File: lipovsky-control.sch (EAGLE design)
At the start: 46 parts, among them J1 JUMPER-PAD, P1 M04-929P, P2 M04-929P, P3 M04-929P, P4 M04-929P, U1 ATTINYX4A8MU, U2 MIC2288YD5, U3 MIC2288YD5, U4 LTV-816S

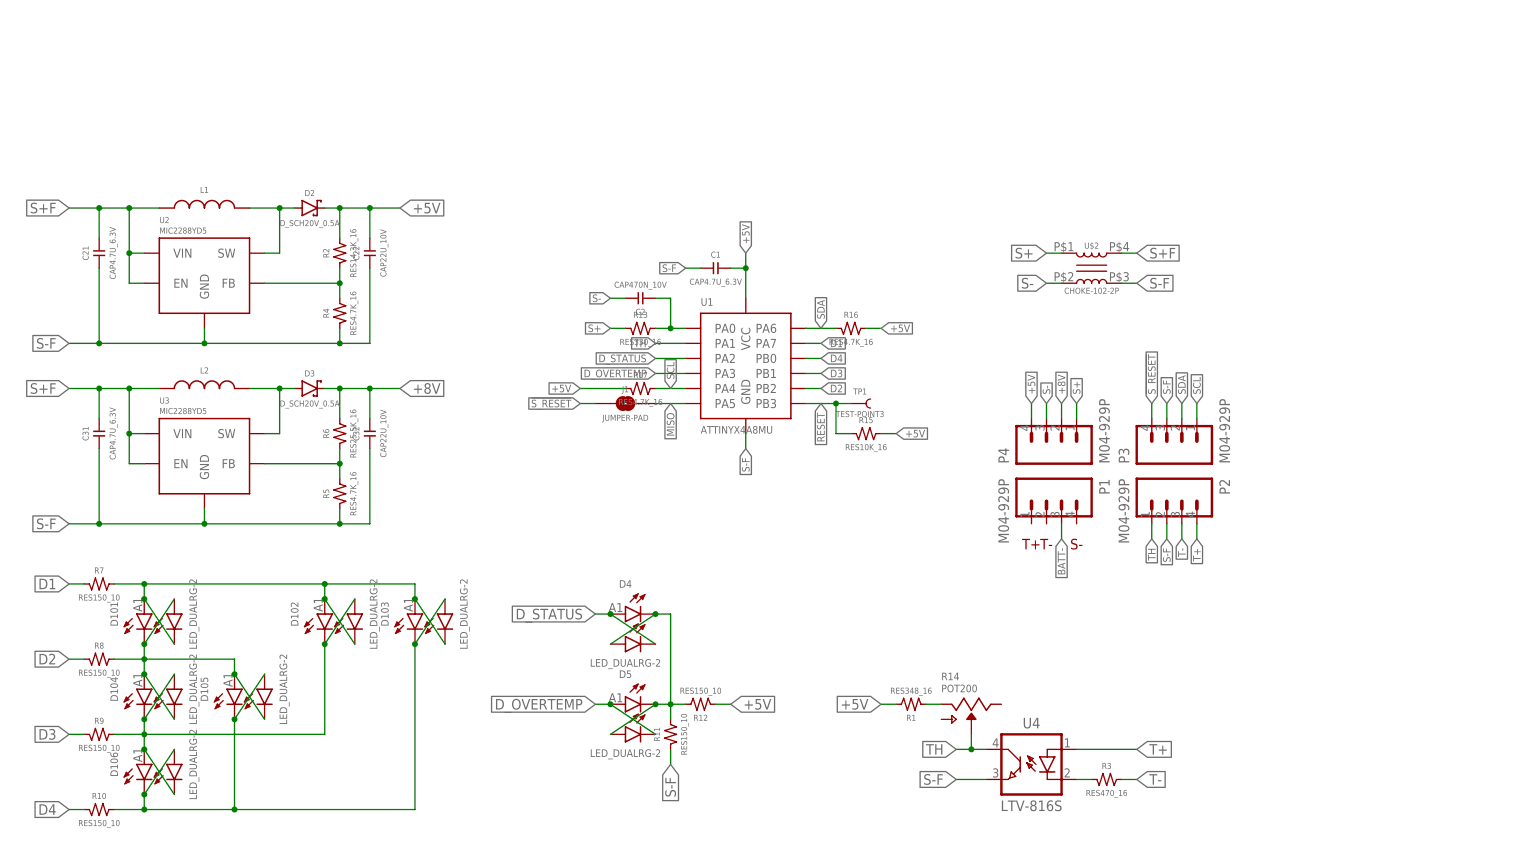
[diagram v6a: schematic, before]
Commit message: prog testpoints
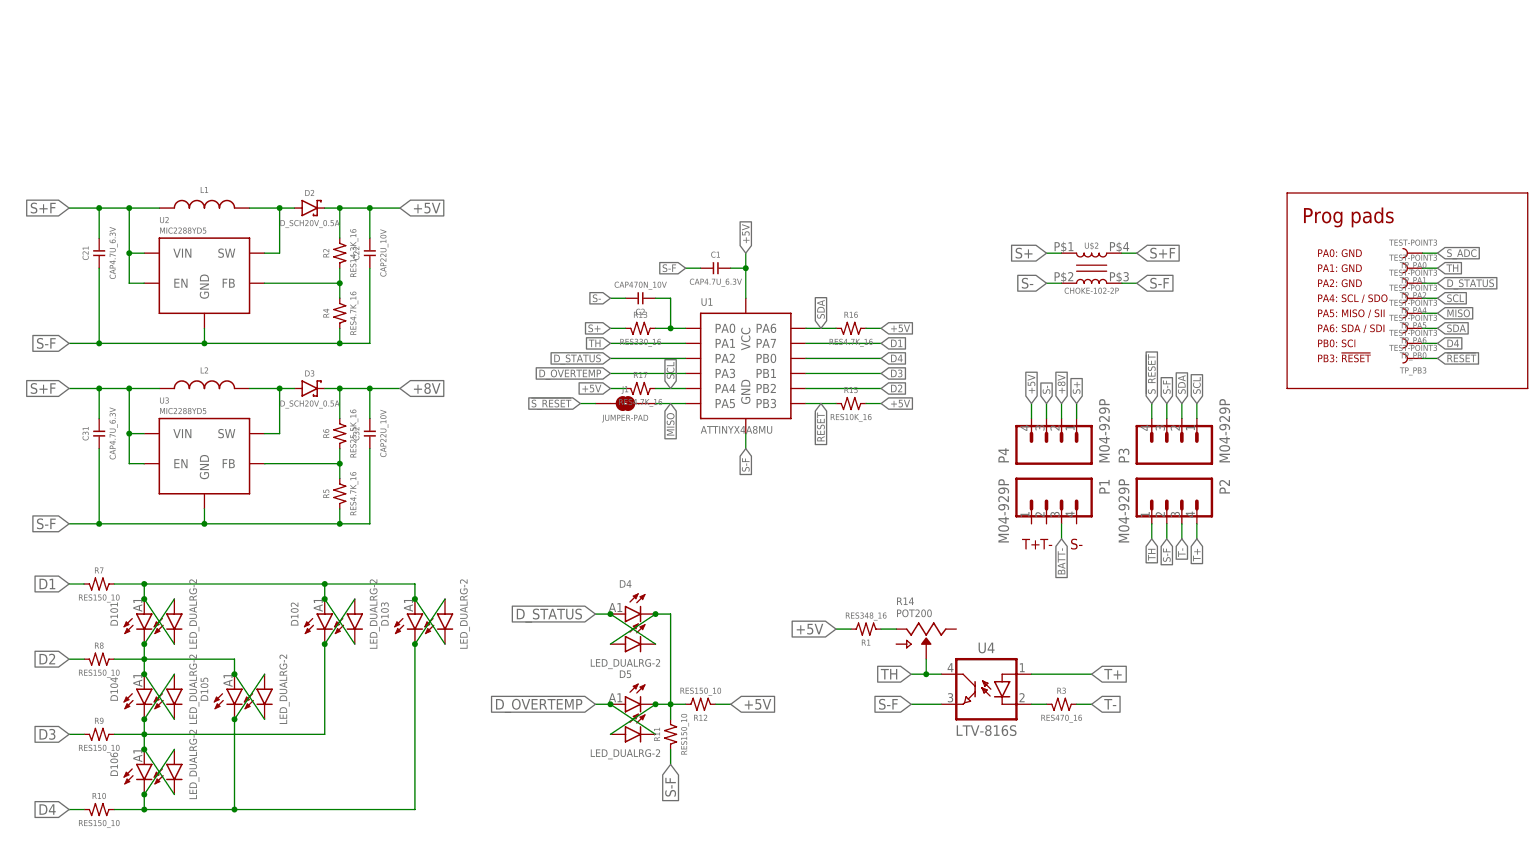
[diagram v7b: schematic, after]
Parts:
- removed TP1: TEST-POINT3, SparkFun-Passives:TEST-POINT3
- added TP_PA0, TP_PA1, TP_PA2, TP_PA4, TP_PA5, TP_PA6, TP_PB0, TP_PB3: TEST-POINT3, SparkFun-Passives:TEST-POINT3
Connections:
- net !RESET: now also TP_PB3.1; no longer TP1.1
- net D4: now also TP_PB0.1
- net D_STATUS: now also TP_PA2.1
- net MISO: now also TP_PA5.1
- net SCL: now also TP_PA4.1
- net SDA: now also TP_PA6.1
- net S_ADC: now also TP_PA0.1
- net TH: now also TP_PA1.1
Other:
- note added: "PA0: GND"
- note added: "PA1: GND"
- note added: "PA2: GND"
- note added: "PA4: SCL / SDO"
- note added: "PA5: MISO / SII"
- note added: "PA6: SDA / SDI"
- note added: "PB0: SCI"
- note added: "PB3: !RESET"
- note added: "Prog pads"
- moved on the sheet: R1, R14, R15, R3, U4

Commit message: ATtiny1616
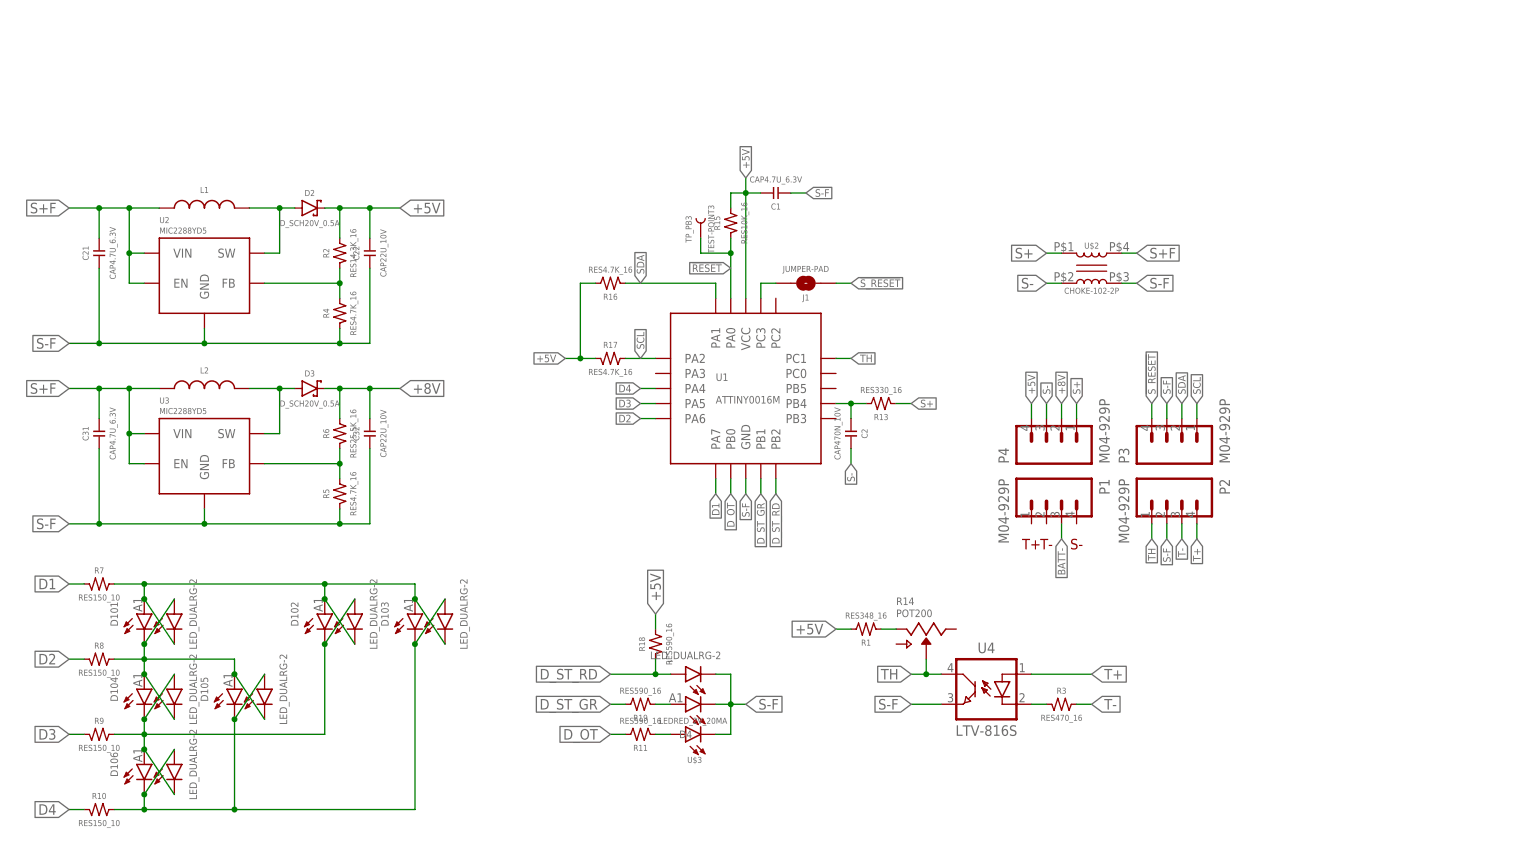
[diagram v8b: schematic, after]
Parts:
- removed D5: LED_DUALRG-2, dubec:LED_DUALRG-2
- removed R12: RES150_10, dubec:RES150_10
- removed TP_PA0, TP_PA1, TP_PA2, TP_PA4, TP_PA5, TP_PA6, TP_PB0: TEST-POINT3, SparkFun-Passives:TEST-POINT3
- added R18, R19: RES590_16, dubec:RES590_16
- added U$3: LEDRED_2V_20MA, dubec:LEDRED_2V_20MA
- R11: value RES150_10 -> RES590_16; device dubec:RES150_10 -> dubec:RES590_16
- U1: value ATTINYX4A8MU -> ATTINY0016M; device dubec:ATTINYX4A8MU -> dubec:ATTINY0016M
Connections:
- removed net D_OVERTEMP: D5.A1, D5.C2, U1.PA3
- removed net D_STATUS: D4.A1, D4.C2, TP_PA2.1, U1.PA2
- removed net MISO: J1.2, TP_PA5.1, U1.PA5
- new net D_OT: R11.2, U1.PB0
- new net D_ST_GR: R19.2, U1.PB1
- new net D_ST_RD: D4.A2, R18.1, U1.PB2
- new net N$3: J1.2, U1.PC3
- new net N$5: D4.A1, R19.1
- net !RESET: now also U1.PA0; no longer U1.PB3
- net +5V: now also R18.2; no longer R12.1
- net D2: now also U1.PA6; no longer U1.PB2
- net D3: now also U1.PA5; no longer U1.PB1
- net D4: now also U1.PA4; no longer TP_PB0.1, U1.PB0
- net N$2: now also R11.1, U$3.A; no longer D4.A2, D4.C1, D5.A2, D5.C1, R11.2, R12.2
- net S-F: now also D4.C1, D4.C2, U$3.C; no longer R11.1
- net SCL: now also U1.PA2; no longer TP_PA4.1, U1.PA4
- net SDA: now also U1.PA1; no longer TP_PA6.1, U1.PA6
- net S_ADC: now also U1.PB4; no longer TP_PA0.1, U1.PA0
- net TH: now also U1.PC1; no longer TP_PA1.1, U1.PA1
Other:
- note removed: "PA0: GND"
- note removed: "PA1: GND"
- note removed: "PA2: GND"
- note removed: "PA4: SCL / SDO"
- note removed: "PA5: MISO / SII"
- note removed: "PA6: SDA / SDI"
- note removed: "PB0: SCI"
- note removed: "PB3: !RESET"
- note removed: "Prog pads"
- moved on the sheet: C1, C2, D4, J1, R11, R13, R15, R16, R17, TP_PB3
